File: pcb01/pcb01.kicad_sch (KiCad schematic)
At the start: 7 parts, among them U1 W65C02SxP, U2 HM62256BLP, U3 27C512, U4 PAL20RS10, U5 74LS138, U6 74HCT574, U7 HM62256BLP

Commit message: more work on pcd layout
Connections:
- net CS_ROM is gone; now on net ~{CS_ROM}: U3.20 (~{CE})
- net ~{CS_RAM1}: now also U4.16 (O7); no longer U4.22 (O1)
- net ~{IO_SEL}: now also U4.22 (O1); no longer U4.16 (O7)
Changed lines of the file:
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@@
-    (effects (font (size 1.27 1.27)) (justify left bottom))
-  )
-  (label "~{CS_RAM1}" (at 63.5 149.86 0) (fields_autoplaced)
     (effects (font (size 1.27 1.27)) (justify left bottom))
   )
@@
     (effects (font (size 1.27 1.27)) (justify right bottom))
   )
-  (label "~{IO_SEL}" (at 63.5 165.1 0) (fields_autoplaced)
-    (effects (font (size 1.27 1.27)) (justify left bottom))
-  )
   (label "~{SYS_CLK}" (at 63.5 154.94 0) (fields_autoplaced)
     (effects (font (size 1.27 1.27)) (justify left bottom))
@@
     (effects (font (size 1.27 1.27)) (justify right bottom))
   )
+  (label "~{CS_RAM1}" (at 63.5 165.1 0) (fields_autoplaced)
+    (effects (font (size 1.27 1.27)) (justify left bottom))
+  )
   (label "A4" (at 204.47 80.01 180) (fields_autoplaced)
     (effects (font (size 1.27 1.27)) (justify right bottom))
@@
     (effects (font (size 1.27 1.27)) (justify left bottom))
   )
+  (label "~{IO_SEL}" (at 63.5 149.86 0) (fields_autoplaced)
+    (effects (font (size 1.27 1.27)) (justify left bottom))
+  )
   (label "~{QOE}" (at 204.47 115.57 180) (fields_autoplaced)
     (effects (font (size 1.27 1.27)) (justify right bottom))
@@
     (effects (font (size 1.27 1.27)) (justify left bottom))
   )
-  (label "CS_ROM" (at 204.47 113.03 180) (fields_autoplaced)
-    (effects (font (size 1.27 1.27)) (justify right bottom))
-  )
+  (label "~{CS_ROM}" (at 204.47 113.03 180) (fields_autoplaced)
+    (effects (font (size 1.27 1.27)) (justify right bottom))
+  )

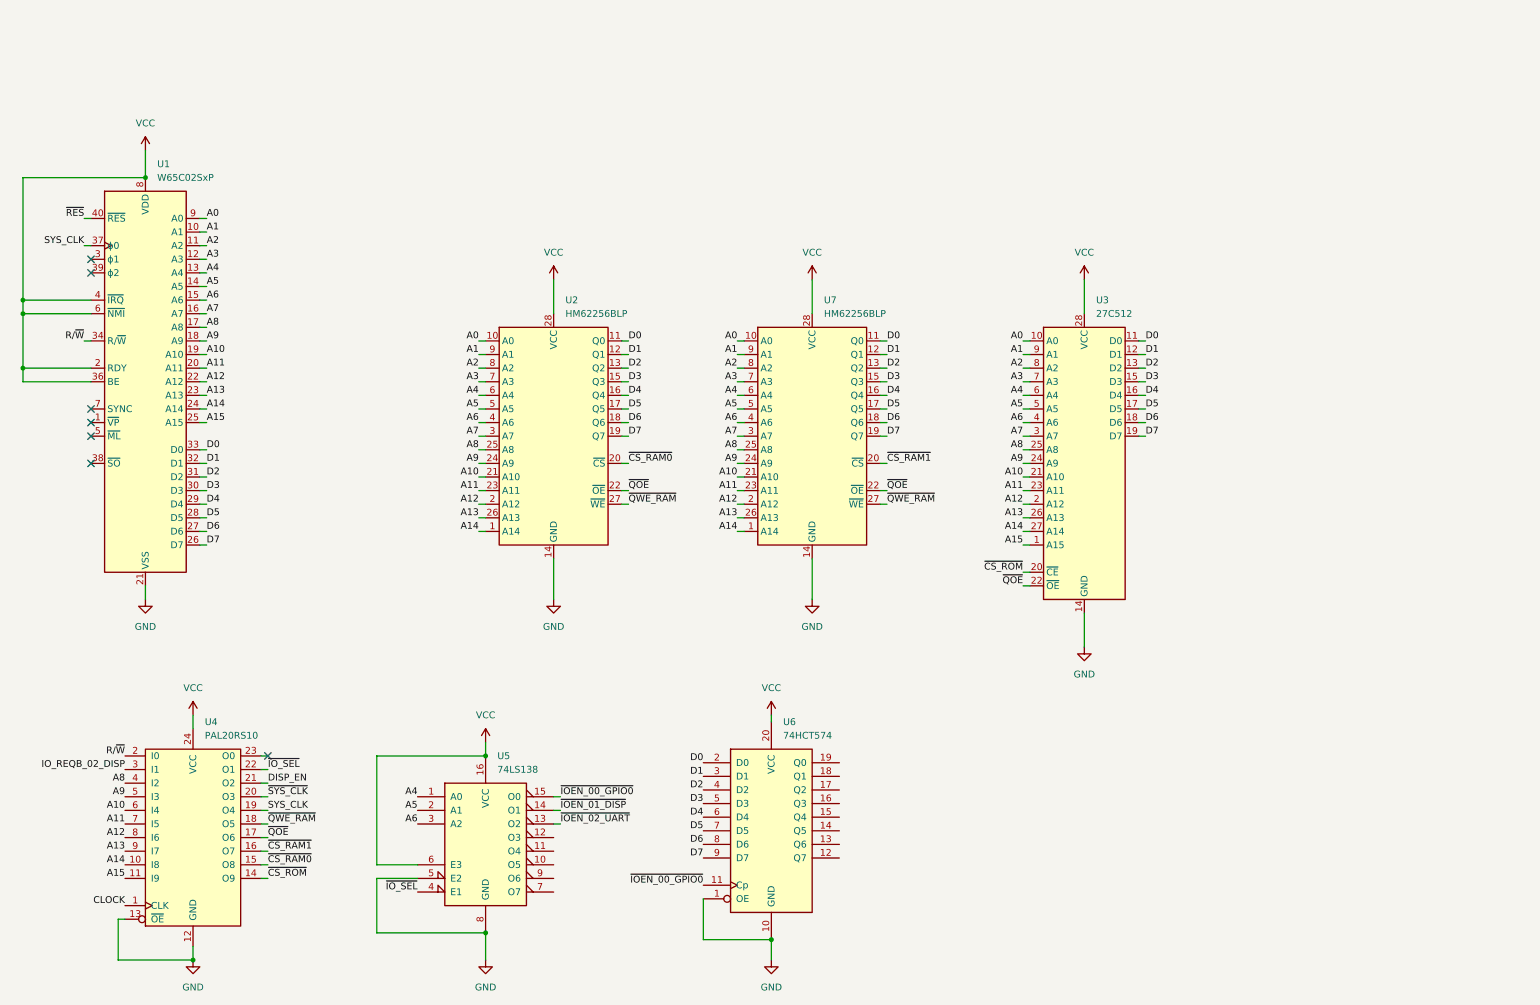
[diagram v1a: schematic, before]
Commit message: wire in the R6552 uart
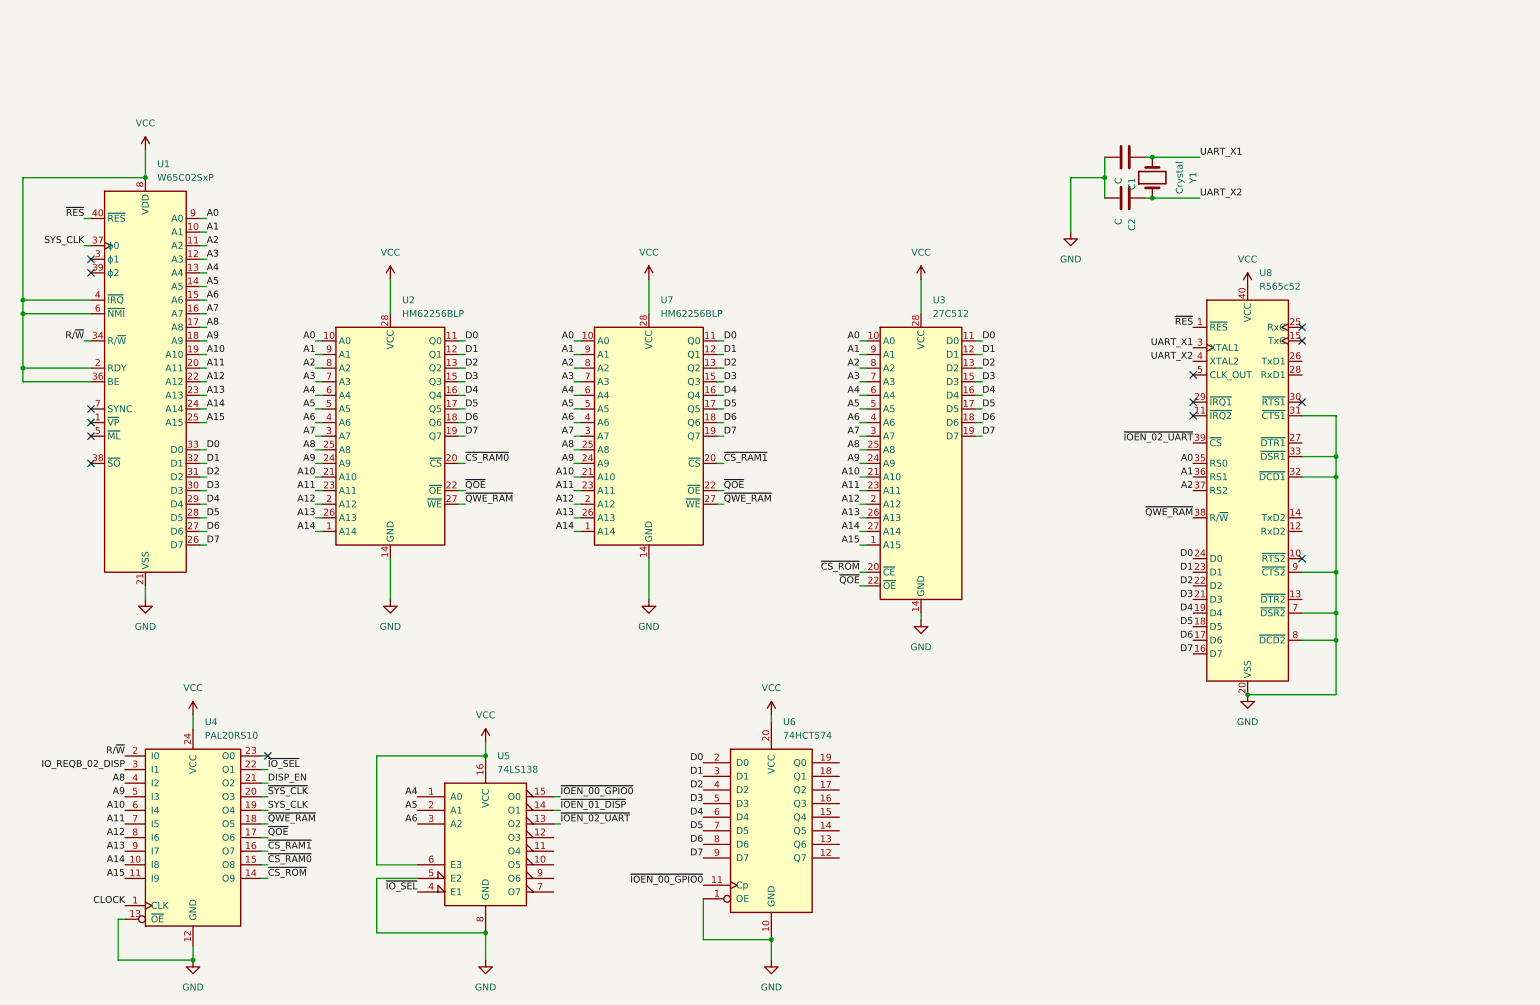
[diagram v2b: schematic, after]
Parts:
- added C1, C2: C, Capacitor_THT:C_Disc_D4.7mm_W2.5mm_P5.00mm, symbol Device:C
- added U8: R565c52, Package_DIP:DIP-40_W15.24mm, symbol 65xx:R565c52
- added Y1: Crystal, Crystal:Crystal_HC49-4H_Vertical, symbol Device:Crystal
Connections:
- net A0: now also U8.35 (RS0)
- net A1: now also U8.36 (RS1)
- net A2: now also U8.37 (RS2)
- net D0: now also U8.24 (D0)
- net D1: now also U8.23 (D1)
- net D2: now also U8.22 (D2)
- net D3: now also U8.21 (D3)
- net D4: now also U8.19 (D4)
- net D5: now also U8.18 (D5)
- net D6: now also U8.17 (D6)
- net D7: now also U8.16 (D7)
- net GND: now also C1.2, C2.2, U8.20 (VSS), U8.31 (~{CTS1}), U8.32 (~{DCD1}), U8.33 (~{DSR1}), U8.7 (~{DSR2}), U8.8 (~{DCD2}), U8.9 (~{CTS2})
- net VCC: now also U8.40 (VCC)
- net ~{IOEN_02_UART}: now also U8.39 (~{CS})
- net ~{QWE_RAM}: now also U8.38 (R/~{W})
- net ~{RES}: now also U8.1 (~{RES})
- new net UART_X1: C1.1, U8.3 (XTAL1), Y1.2
- new net UART_X2: C2.1, U8.4 (XTAL2), Y1.1
- no-connect marks 7 -> 14
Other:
- moved on the sheet: U2, U3, U7

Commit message: add reset circuit and filter caps
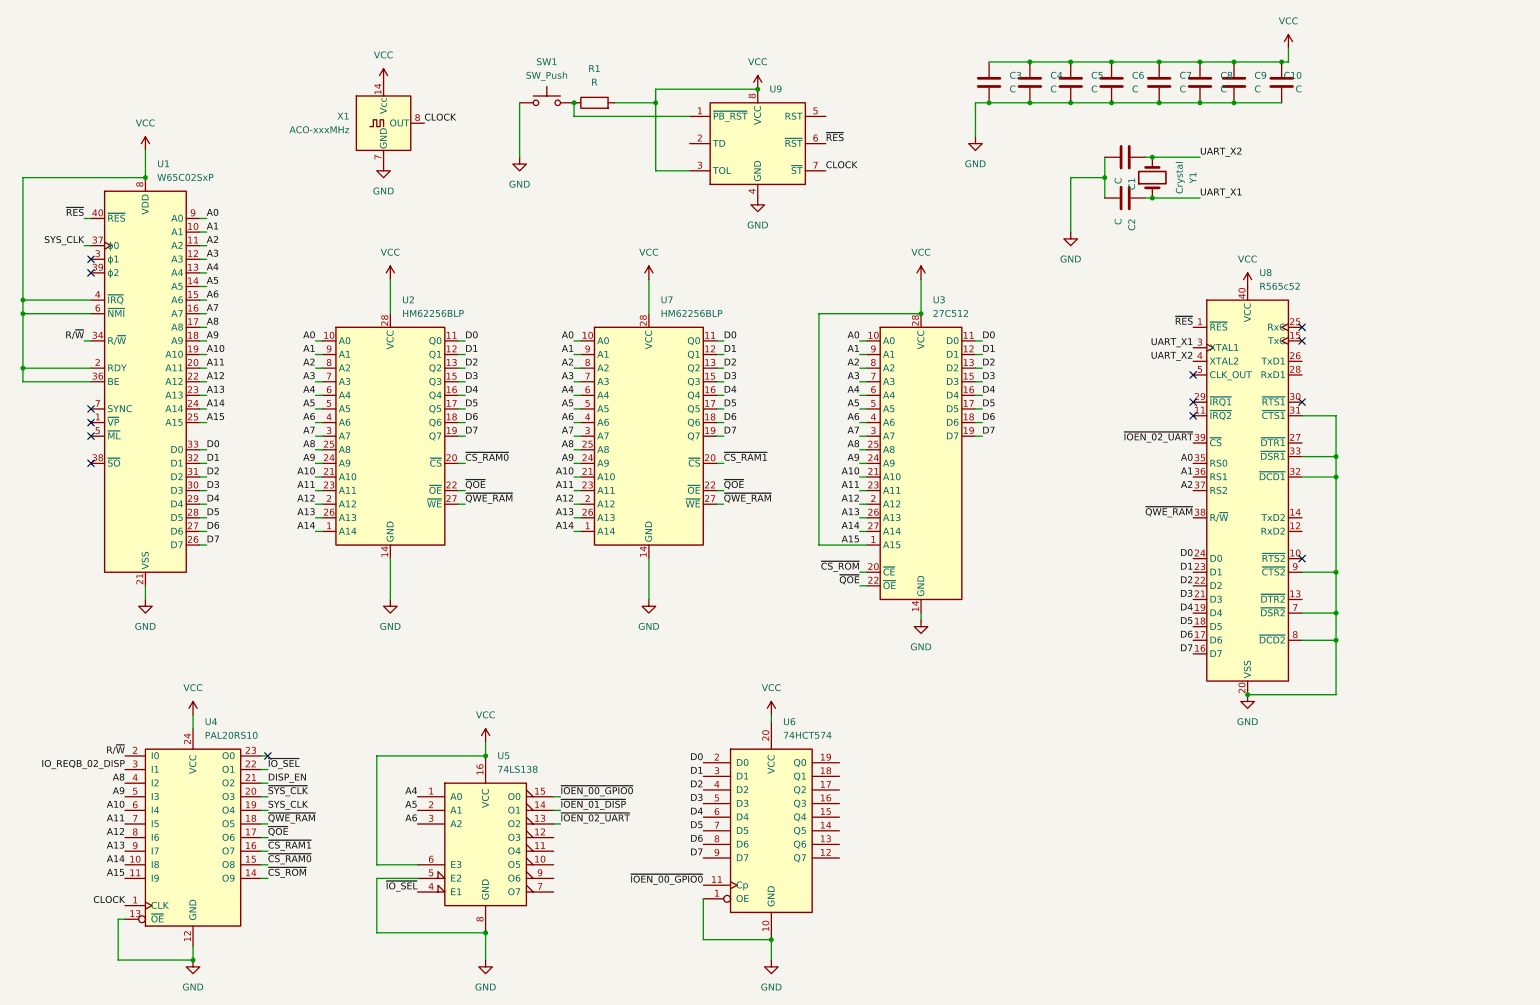
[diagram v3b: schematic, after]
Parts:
- added C10, C3, C4, C5, C6, C7, C8, C9: C, Capacitor_THT:C_Disc_D4.7mm_W2.5mm_P5.00mm, symbol Device:C
- added R1: R, Resistor_THT:R_Axial_DIN0207_L6.3mm_D2.5mm_P7.62mm_Horizontal, symbol Device:R
- added SW1: SW_Push, Button_Switch_THT:SW_TH_Tactile_Omron_B3F-10xx, symbol Switch:SW_Push
- added U9: ~, Package_SO:SO-8_3.9x4.9mm_P1.27mm, symbol 65xx:TC1232
- added X1: ACO-xxxMHz, Oscillator:Oscillator_DIP-14, symbol Oscillator:ACO-xxxMHz
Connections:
- net A15 is gone; now on net VCC: U1.25 (A15), U3.1 (A15), U4.11 (I9)
- net CLOCK: now also U9.7 (~{ST}), X1.8 (OUT)
- net GND: now also C10.2, C3.2, C4.2, C5.2, C6.2, C7.2, C8.2, C9.2, SW1.2, U9.4 (GND), X1.7 (GND)
- net UART_X1: now also C2.1, Y1.1; no longer C1.1, Y1.2
- net UART_X2: now also C1.1, Y1.2; no longer C2.1, Y1.1
- net VCC: now also C10.1, C3.1, C4.1, C5.1, C6.1, C7.1, C8.1, C9.1, R1.2, U9.3 (TOL), U9.8 (VCC), X1.14 (Vcc)
- net ~{RES}: now also U9.6 (~{RST})
- new net: R1.1, SW1.1, U9.1 (~{PB_RST})

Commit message: pcb layout should be finished...
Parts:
- added J1: DIN41612_02x32_AC, Connector_DIN:DIN41612_C_2x32_Male_Horizontal_THT, symbol Connector:DIN41612_02x32_AC
- added J2: Conn_01x08_Socket, Connector_PinSocket_2.54mm:PinSocket_1x08_P2.54mm_Vertical, symbol Connector:Conn_01x08_Socket
- added J3: Conn_01x16_Socket, Connector_PinSocket_2.54mm:PinSocket_1x16_P2.54mm_Vertical, symbol Connector:Conn_01x16_Socket
- X1: footprint Oscillator:Oscillator_DIP-14 -> Package_DIP:DIP-14_W7.62mm; symbol Oscillator:ACO-xxxMHz -> 65xx:osci-14or8
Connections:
- net A0: now also J1.c31 (Pin_c31), J3.1 (Pin_1)
- net A1: now also J1.c30 (Pin_c30), J3.2 (Pin_2)
- net A10: now also J1.c21 (Pin_c21), J3.11 (Pin_11)
- net A11: now also J1.c20 (Pin_c20), J3.12 (Pin_12)
- net A12: now also J1.c19 (Pin_c19), J3.13 (Pin_13)
- net A13: now also J1.c18 (Pin_c18), J3.14 (Pin_14)
- net A14: now also J1.c17 (Pin_c17), J3.15 (Pin_15)
- net A2: now also J1.c29 (Pin_c29), J3.3 (Pin_3)
- net A3: now also J1.c28 (Pin_c28), J3.4 (Pin_4)
- net A4: now also J1.c27 (Pin_c27), J3.5 (Pin_5)
- net A5: now also J1.c26 (Pin_c26), J3.6 (Pin_6)
- net A6: now also J1.c25 (Pin_c25), J3.7 (Pin_7)
- net A7: now also J1.c24 (Pin_c24), J3.8 (Pin_8)
- net A8: now also J1.c23 (Pin_c23), J3.9 (Pin_9)
- net A9: now also J1.c22 (Pin_c22), J3.10 (Pin_10)
- net D0: now also J1.c9 (Pin_c9), J2.1 (Pin_1)
- net D1: now also J1.c8 (Pin_c8), J2.2 (Pin_2)
- net D2: now also J1.c7 (Pin_c7), J2.3 (Pin_3)
- net D3: now also J1.c6 (Pin_c6), J2.4 (Pin_4)
- net D4: now also J1.c5 (Pin_c5), J2.5 (Pin_5)
- net D5: now also J1.c4 (Pin_c4), J2.6 (Pin_6)
- net D6: now also J1.c3 (Pin_c3), J2.7 (Pin_7)
- net D7: now also J1.c2 (Pin_c2), J2.8 (Pin_8)
- net GND: now also J1.c1 (Pin_c1), J1.c15 (Pin_c15), J1.c32 (Pin_c32)
- net SYS_CLK: now also J1.a3 (Pin_a3)
- net VCC: now also X1.11 (Vcc), J1.a1 (Pin_a1), J1.a15 (Pin_a15), J1.a32 (Pin_a32); no longer U1.25 (A15), U4.11 (I9)
- net ~{IO_SEL}: now also J1.a23 (Pin_a23)
- net ~{QOE}: now also J1.a5 (Pin_a5)
- net ~{QWE_RAM}: now also J1.a4 (Pin_a4)
- net ~{RES}: now also J1.a2 (Pin_a2)
- net ~{IOEN_05}: now reaches U5.10 (O5)
- net ~{IOEN_05}: now also J1.a26 (Pin_a26)
- net ~{IOEN_04}: now reaches U5.11 (O4)
- net ~{IOEN_04}: now also J1.a27 (Pin_a27)
- net ~{IOEN_03}: now reaches U5.12 (O3)
- net ~{IOEN_03}: now also J1.a28 (Pin_a28)
- net ~{IOEN_07}: now reaches U5.7 (O7)
- net ~{IOEN_07}: now also J1.a24 (Pin_a24)
- net ~{IOEN_06}: now reaches U5.9 (O6)
- net ~{IOEN_06}: now also J1.a25 (Pin_a25)
- new net A15: J1.c16 (Pin_c16), J3.16 (Pin_16), U1.25 (A15), U4.11 (I9)
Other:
- moved on the sheet: U8
